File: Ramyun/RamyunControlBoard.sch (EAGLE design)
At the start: 7 parts, among them IC1 MCP23017SO, X1 5267-02, X2 5267-03

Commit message: tired
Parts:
- added C2: (no value), adafruit:CPOL-USE3.5-8
- added C3: 0.1uF, GFE:C0603(1608)_HAND
- added H1, H2, H3, H4: MOUNT-HOLE4.1, holes:MOUNT-HOLE4.1
- added J1, J2: (no value), SparkFun-Connectors:CONN_08X2
- added JP1: M02PTH, berry:M02PTH
- added LED2: (no value), GFE:LED3MM
- added LOGO1: GRADEFREELOGO-20, GFE:GRADEFREELOGO-20
- added Q1: NVF6P02, GFE:NVF6P02
- added Q2: BC817-16LT1SMD, GFE:BC817-16LT1SMD
- added R10, R11: 100k, GFE:R0603(1608)_HAND
- added R12, R13, R14, R15, R16, R17, R18, R19, R2, R20, R3, R4, R5, R8: 4.7k, GFE:R0603(1608)_HAND
- added R21, R39, R9: 500, GFE:R0603(1608)_HAND
- added R22, R23, R24, R25, R26, R27, R28, R29, R30, R31, R32, R33, R34, R35, R36, R37: 470, GFE:R0603(1608)_HAND
- added R38: 1k, GFE:R0603(1608)_HAND
- added R6, R7: 390, GFE:R0603(1608)_HAND
- added U1: LMP7702, GFE:LMP7702
- added X10, X11, X16, X3, X4, X5, X6, X7, X8, X9: 5267-02, GFE:5267-02
- added X12, X13, X14, X15, X17: 5267-03, GFE:5267-03
- C1: value (none) -> 0.1uF
- R1: value (none) -> 4.7k
- X2: value 5267-03 -> 5267-02; device GFE:5267-03 -> GFE:5267-02
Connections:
- new net +5V: C2.+, Q1.S, R21.2, X12.1, X13.1
- new net ANALOG_1: MS1.GPIOA0, U1A.-IN, U1A.OUT
- new net ANALOG_2: MS1.GPIOA1, U1B.-IN, U1B.OUT
- new net BTN_1: R20.2, X1.1
- new net BTN_10: R3.1, X10.1
- new net BTN_11: R4.1, X11.1
- new net BTN_2: R19.2, X2.1
- new net BTN_3: R18.2, X3.1
- new net BTN_4: R17.2, X4.1
- new net BTN_5: R16.2, X5.1
- new net BTN_6: R15.2, X6.1
- new net BTN_7: R14.2, X7.1
- new net BTN_8: R1.1, X8.1
- new net BTN_9: R2.1, X9.1
- new net EXT_5V: Q1.D, X16.1
- new net IO_1: J2.15, R30.2
- new net IO_10: J1.13, R23.2
- new net IO_11: J1.11, R24.2
- new net IO_12: J1.9, R25.2
- new net IO_13: J1.7, R26.2
- new net IO_14: J1.5, R27.2
- new net IO_15: J1.3, R28.2
- new net IO_16: J1.1, R29.2
- new net IO_2: J2.13, R31.2
- new net IO_3: J2.11, R32.2
- new net IO_4: J2.9, R33.2
- new net IO_5: J2.7, R34.2
- new net IO_6: J2.5, R35.2
- new net IO_7: J2.3, R36.2
- new net IO_8: J2.1, R37.2
- new net IO_9: J1.15, R22.2
- new net LED_1: MS1.GPIO13, R38.1
- new net N$1: MS1.GPIOA2, R20.1
- new net N$10: MS1.GPIO6, R2.2
- new net N$11: MS1.GPIO9, R3.2
- new net N$12: MS1.GPIO10, R4.2
- new net N$13: MS1.GPIOTX, R12.1
- new net N$14: MS1.GPIORX, R13.1
- new net N$15: MS1.GPIOSCK, R16.1
- new net N$16: MS1.GPIOMOSI, R15.1
- new net N$17: MS1.GPIOMISO, R14.1
- new net N$18: IC1.GPA0, R30.1
- new net N$19: IC1.GPA1, R31.1
- new net N$2: R10.2, U1A.+IN
- new net N$20: IC1.GPA2, R32.1
- new net N$21: IC1.GPA3, R33.1
- new net N$22: IC1.GPA4, R34.1
- new net N$23: IC1.GPA5, R35.1
- new net N$24: IC1.GPA6, R36.1
- new net N$25: IC1.GPA7, R37.1
- new net N$26: IC1.GPB0, R22.1
- new net N$27: IC1.GPB1, R23.1
- new net N$28: IC1.GPB2, R24.1
- new net N$29: IC1.GPB3, R25.1
- new net N$3: R11.2, U1B.+IN
- new net N$30: IC1.GPB4, R26.1
- new net N$31: IC1.GPB5, R27.1
- new net N$32: IC1.GPB6, R28.1
- new net N$33: IC1.GPB7, R29.1
- new net N$34: R6.1, X12.2
- new net N$35: R7.1, X13.2
- new net N$36: LED2.A, R21.1
- new net N$4: MS1.GPIOA3, R19.1
- new net N$5: MS1.GPIOA4, R18.1
- new net N$50: Q2.C, R39.1
- new net N$51: Q2.B, R38.2
- new net N$52: JP1.2, R39.2
- new net N$53: LED1.A, R9.1
- new net N$6: MS1.GPIOA5, R17.1
- new net N$7: R11.1, X15.2
- new net N$8: R10.1, X14.2
- new net N$9: MS1.GPIO5, R1.2
- new net RXD: R13.2, X17.3
- new net SCL: IC1.SCL, MS1.GPIOSCL, R8.1
- new net SDA: IC1.SDA, MS1.GPIOSDA, R5.1
- new net SERVO_1: MS1.GPIO11, R6.2
- new net SERVO_2: MS1.GPIO12, R7.2
- new net TXD: R12.2, X17.2
- net 3.3V: now also C1.1, C3.1, IC1.!RESET, IC1.VDD, R5.2, R8.2, R9.2, U1G$2.V+, X14.1, X15.1
- net GND: now also C1.2, C2.-, C3.2, IC1.A0, IC1.A1, IC1.A2, IC1.VSS, J1.10, J1.12, J1.14, J1.16, J1.2, J1.4, J1.6, J1.8, J2.10, J2.12, J2.14, J2.16, J2.2, J2.4, J2.6, J2.8, LED1.C, LED2.C, Q1.G, Q2.E, U1G$2.V-, X1.2, X10.2, X11.2, X12.3, X13.3, X14.3, X15.3, X16.2, X17.1, X2.2, X3.2, X4.2, X5.2, X6.2, X7.2, X8.2, X9.2
- net VBUS: now also JP1.1
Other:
- note added: "5V reverse voltage protection"
- note added: "TODO: capacitor for servo!"
- moved on the sheet: C1, LED1, R1, X1

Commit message: tired 2
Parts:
- added TP1, TP2: (no value), berry:TP-5010
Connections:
- net +5V: now also TP1.TP
- net GND: now also TP2.TP
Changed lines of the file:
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@@
 <part name="GND28" library="GFE" deviceset="GND" device=""/>
 <part name="H4" library="holes" deviceset="MOUNT-HOLE" device="4.1"/>
+<part name="TP1" library="berry" deviceset="TP" device="-5010"/>
+<part name="TP2" library="berry" deviceset="TP" device="-5010"/>
+<part name="P+5" library="supply1" deviceset="+5V" device=""/>
+<part name="GND29" library="GFE" deviceset="GND" device=""/>
 </parts>
 <sheets>
@@
 <instance part="GND28" gate="1" x="355.6" y="111.76" rot="R90"/>
 <instance part="H4" gate="G$1" x="266.7" y="12.7"/>
+<instance part="TP1" gate="G$1" x="180.34" y="91.44"/>
+<instance part="TP2" gate="G$1" x="195.58" y="91.44"/>
+<instance part="P+5" gate="1" x="175.26" y="83.82" rot="R90"/>
+<instance part="GND29" gate="1" x="200.66" y="83.82" rot="R90"/>
 </instances>
 <busses>
@@
 <pinref part="GND28" gate="1" pin="GND"/>
 </segment>
+<segment>
+<pinref part="GND29" gate="1" pin="GND"/>
+<pinref part="TP2" gate="G$1" pin="TP"/>
+<wire x1="198.12" y1="83.82" x2="195.58" y2="83.82" width="0.1524" layer="91"/>
+<wire x1="195.58" y1="83.82" x2="195.58" y2="88.9" width="0.1524" layer="91"/>
+</segment>
 </net>
 <net name="N$2" class="0">
@@
 <wire x1="109.22" y1="30.48" x2="109.22" y2="33.02" width="0.1524" layer="91"/>
 </segment>
-</net>
+<segment>
+<pinref part="P+5" gate="1" pin="+5V"/>
+<pinref part="TP1" gate="G$1" pin="TP"/>
+<wire x1="177.8" y1="83.82" x2="180.34" y2="83.82" width="0.1524" layer="91"/>
+<wire x1="180.34" y1="83.82" x2="180.34" y2="88.9" width="0.1524" layer="91"/>
+</segment>
+</net>

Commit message: gerber done
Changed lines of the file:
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@@
 <instance part="IC1" gate="G$1" x="279.4" y="132.08"/>
 <instance part="VBUS1" gate="G$1" x="124.46" y="129.54" rot="R90"/>
-<instance part="3.3V7" gate="G$1" x="185.42" y="119.38"/>
+<instance part="3.3V7" gate="G$1" x="187.96" y="116.84" rot="R270"/>
 <instance part="GND20" gate="1" x="190.5" y="121.92" rot="R90"/>
 <instance part="X1" gate="G$1" x="30.48" y="218.44" rot="R180"/>
@@
 <pinref part="MS1" gate="G$1" pin="3V"/>
 <pinref part="3.3V7" gate="G$1" pin="3.3V"/>
-<wire x1="175.26" y1="116.84" x2="185.42" y2="116.84" width="0.1524" layer="91"/>
-<wire x1="185.42" y1="116.84" x2="185.42" y2="119.38" width="0.1524" layer="91"/>
+<wire x1="175.26" y1="116.84" x2="187.96" y2="116.84" width="0.1524" layer="91"/>
 </segment>
 <segment>

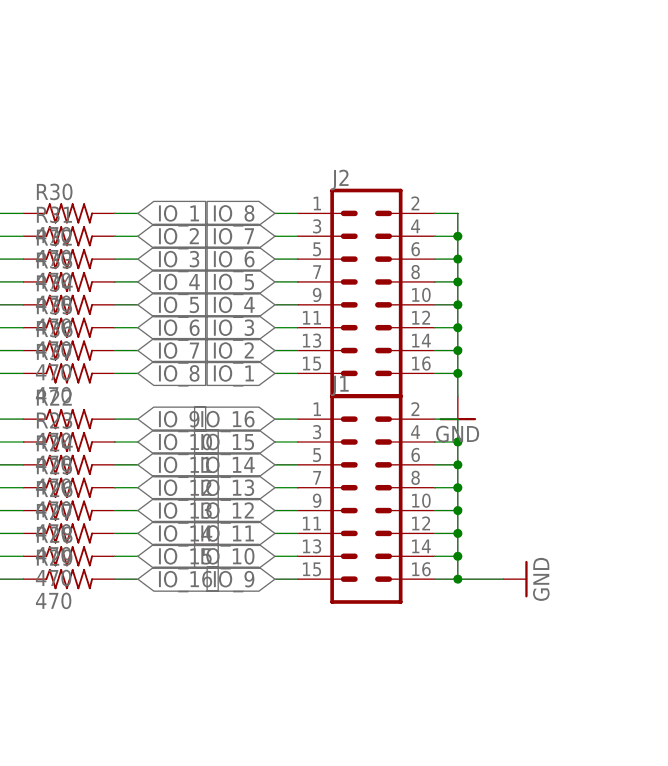
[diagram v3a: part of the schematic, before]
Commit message: nl17sz17
package added
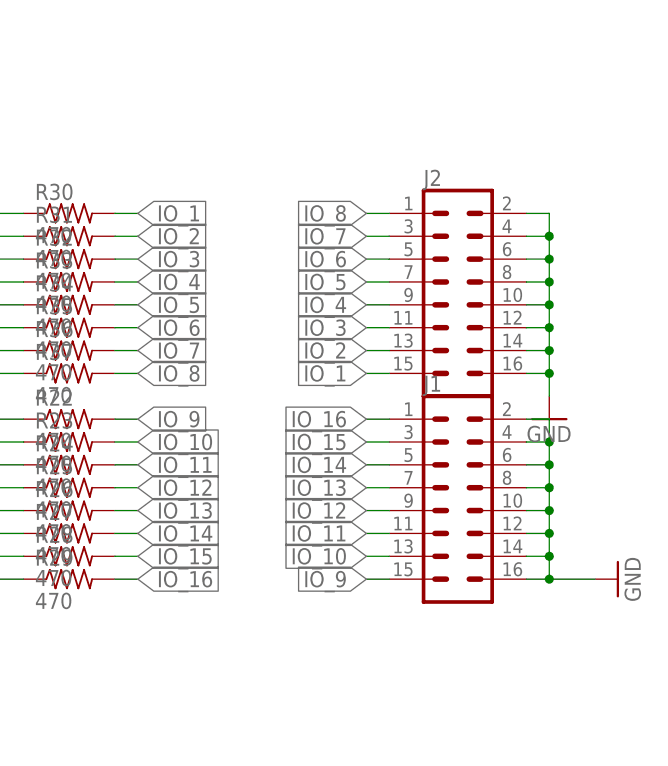
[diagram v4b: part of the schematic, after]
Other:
- moved on the sheet: J1, J2
